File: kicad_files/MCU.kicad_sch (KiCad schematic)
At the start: 27 parts, among them J1 Conn_01x01_Socket, J2 Conn_01x01_Socket, J3 Conn_01x01_Socket, SW1 BOOT BUTTON, SW2 SW_Push, U1 STM32F407VGTx, Y1 LFXTAL036869Reel 8MHz Crystal

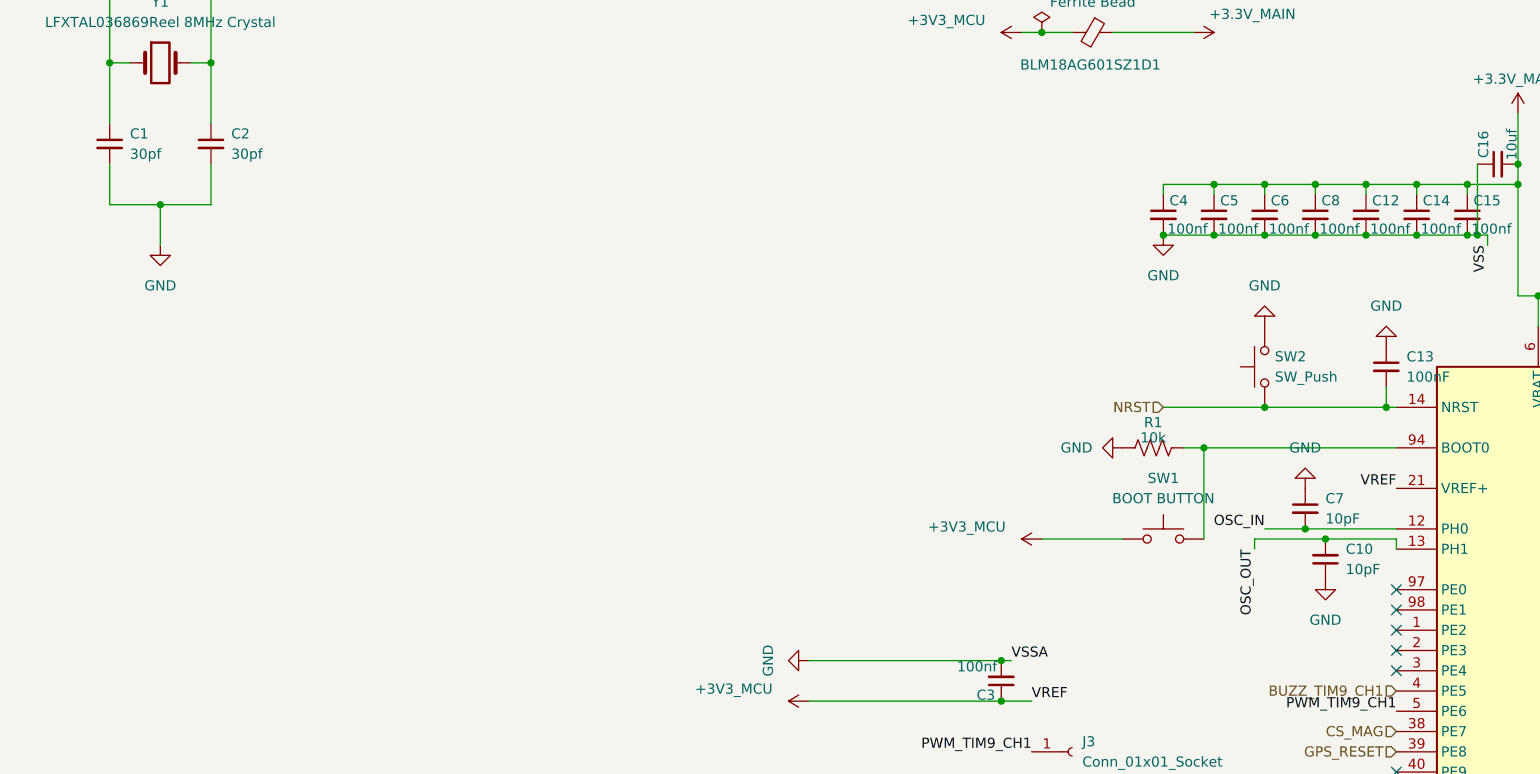
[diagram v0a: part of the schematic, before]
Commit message: rm 10pf caps, add 33pf caps close to mcu pins
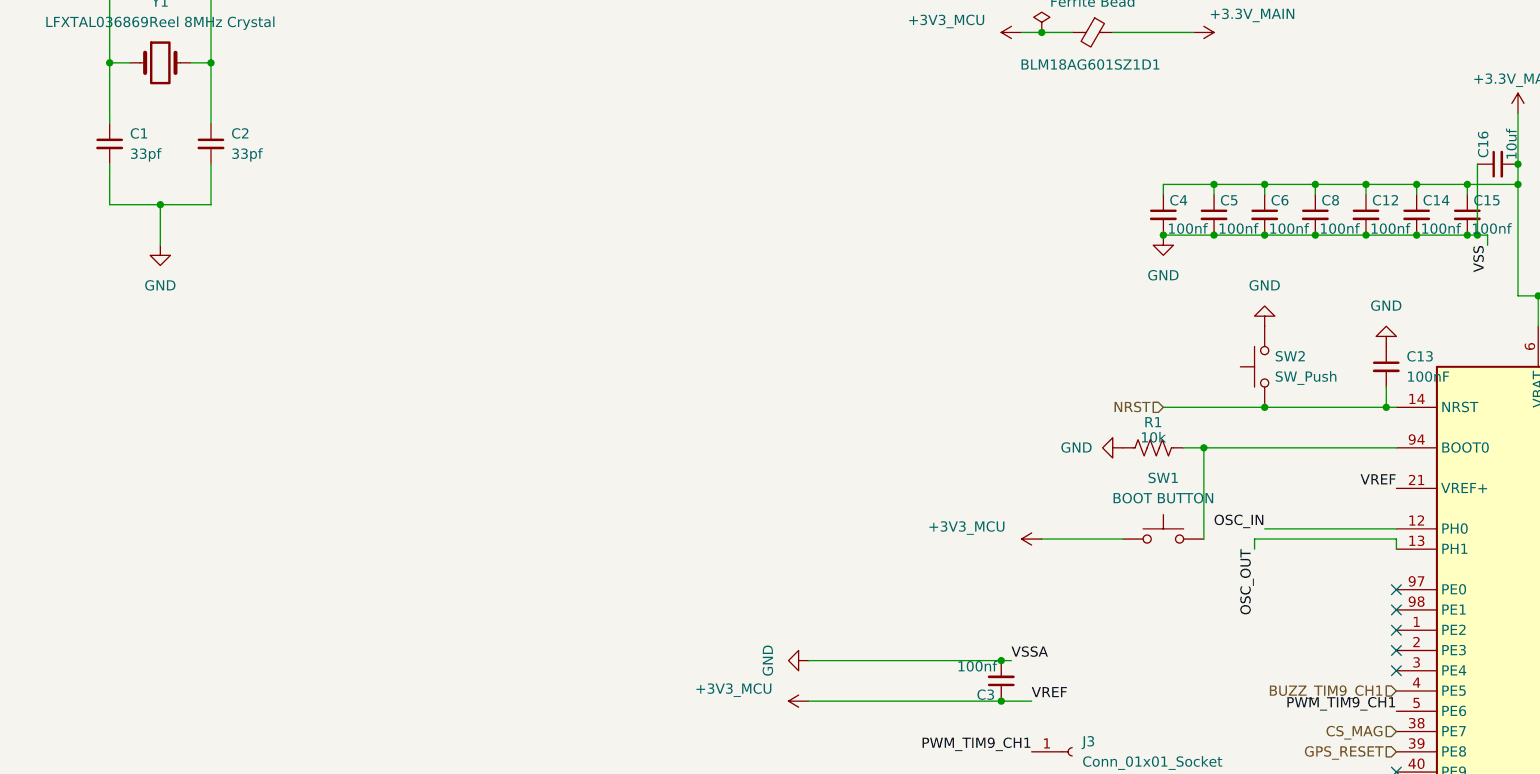
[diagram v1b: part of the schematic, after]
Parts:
- removed C10, C7: 10pF, Capacitor_SMD:C_0402_1005Metric, symbol Device:C_Small
- C1, C2: value 30pf -> 33pf

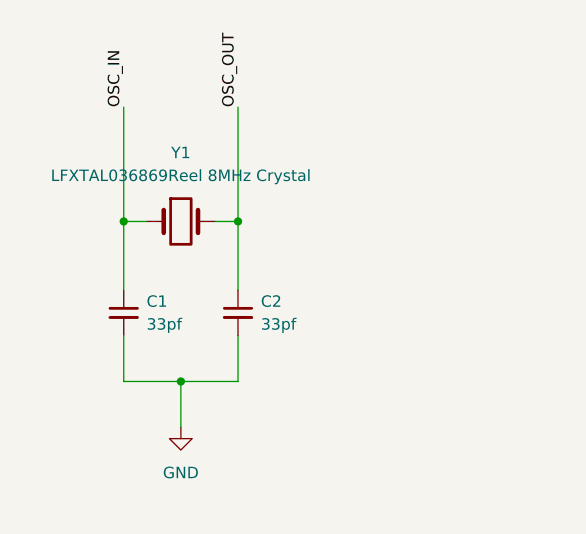
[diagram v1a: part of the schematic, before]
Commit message: replace crystal with smaller, lower esr one, redo footprints, traces
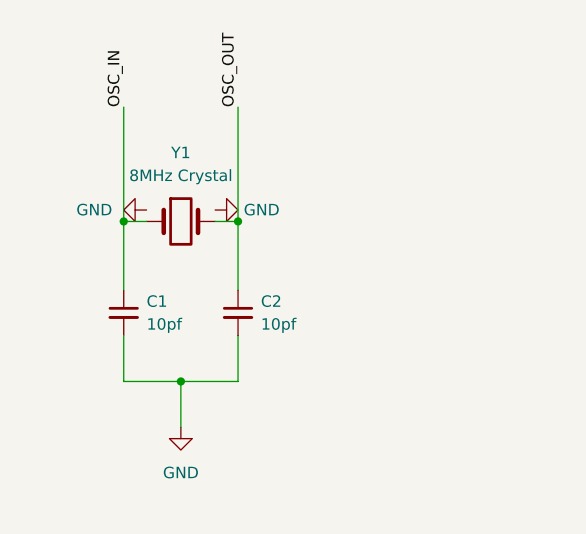
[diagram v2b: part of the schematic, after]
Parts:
- C1, C2: value 33pf -> 10pf
- Y1: value LFXTAL036869Reel 8MHz Crystal -> 8MHz Crystal; footprint Crystal:Crystal_SMD_HC49-SD -> Crystal:Crystal_SMD_3225-4Pin_3.2x2.5mm
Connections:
- net GND: now also Y1.2, Y1.4
- net OSC_OUT: now also Y1.3; no longer Y1.2
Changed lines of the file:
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@@
 			)
 		)
-		(property "Value" "33pf"
+		(property "Value" "10pf"
 			(at 40.64 62.2362 0)
 			(show_name no)
@@
 	)
 	(symbol
+		(lib_id "power:GND")
+		(at 48.26 49.53 90)
+		(unit 1)
+		(body_style 1)
+		(exclude_from_sim no)
+		(in_bom yes)
+		(on_board yes)
+		(in_pos_files yes)
+		(dnp no)
+		(fields_autoplaced yes)
+		(property "Reference" "#PWR010"
+			(at 54.61 49.53 0)
+			(hide yes)
+			(show_name no)
+			(do_not_autoplace no)
+			(effects
+				(font
+					(size 1.27 1.27)
+				)
+			)
+		)
+		(property "Value" "GND"
+			(at 51.435 49.5299 90)
+			(show_name no)
+			(do_not_autoplace no)
+			(effects
+				(font
+					(size 1.27 1.27)
+				)
+				(justify right)
+			)
+		)
+		(property "Footprint" ""
+			(at 48.26 49.53 0)
+			(hide yes)
+			(show_name no)
+			(do_not_autoplace no)
+			(effects
+				(font
+					(size 1.27 1.27)
+				)
+			)
+		)
+		(property "Datasheet" ""
+			(at 48.26 49.53 0)
+			(hide yes)
+			(show_name no)
+			(do_not_autoplace no)
+			(effects
+				(font
+					(size 1.27 1.27)
+				)
+			)
+		)
+		(property "Description" "Power symbol creates a global label with name \"GND\" , ground"
+			(at 48.26 49.53 0)
+			(hide yes)
+			(show_name no)
+			(do_not_autoplace no)
+			(effects
+				(font
+					(size 1.27 1.27)
+				)
+			)
+		)
+		(pin "1"
+		)
+		(instances
+			(project "versorlite"
+				(path "/1a230af0-0a74-48f7-8607-b087121dda49/a6e36be3-aff5-4566-a903-d81edfd88a96"
+					(reference "#PWR010")
+					(unit 1)
+				)
+			)
+		)
+	)
+	(symbol
 		(lib_id "power:+3.3V")
 		(at 173.99 46.99 270)
@@
 	)
 	(symbol
+		(lib_id "power:GND")
+		(at 40.64 49.53 270)
+		(unit 1)
+		(body_style 1)
+		(exclude_from_sim no)
+		(in_bom yes)
+		(on_board yes)
+		(in_pos_files yes)
+		(dnp no)
+		(fields_autoplaced yes)
+		(property "Reference" "#PWR011"
+			(at 34.29 49.53 0)
+			(hide yes)
+			(show_name no)
+			(do_not_autoplace no)
+			(effects
+				(font
+					(size 1.27 1.27)
+				)
+			)
+		)
+		(property "Value" "GND"
+			(at 36.83 49.5299 90)
+			(show_name no)
+			(do_not_autoplace no)
+			(effects
+				(font
+					(size 1.27 1.27)
+				)
+				(justify right)
+			)
+		)
+		(property "Footprint" ""
+			(at 40.64 49.53 0)
+			(hide yes)
+			(show_name no)
+			(do_not_autoplace no)
+			(effects
+				(font
+					(size 1.27 1.27)
+				)
+			)
+		)
+		(property "Datasheet" ""
+			(at 40.64 49.53 0)
+			(hide yes)
+			(show_name no)
+			(do_not_autoplace no)
+			(effects
+				(font
+					(size 1.27 1.27)
+				)
+			)
+		)
+		(property "Description" "Power symbol creates a global label with name \"GND\" , ground"
+			(at 40.64 49.53 0)
+			(hide yes)
+			(show_name no)
+			(do_not_autoplace no)
+			(effects
+				(font
+					(size 1.27 1.27)
+				)
+			)
+		)
+		(pin "1"
+		)
+		(instances
+			(project "versorlite"
+				(path "/1a230af0-0a74-48f7-8607-b087121dda49/a6e36be3-aff5-4566-a903-d81edfd88a96"
+					(reference "#PWR011")
+					(unit 1)
+				)
+			)
+		)
+	)
+	(symbol
 		(lib_id "Connector:Conn_01x01_Socket")
 		(at 158.115 152.4 0)
@@
 			)
 		)
-		(property "Value" "LFXTAL036869Reel 8MHz Crystal"
+		(property "Value" "8MHz Crystal"
 			(at 44.45 45.72 0)
 			(show_name no)
@@
 			)
 		)
-		(property "Footprint" "Crystal:Crystal_SMD_HC49-SD"
+		(property "Footprint" "Crystal:Crystal_SMD_3225-4Pin_3.2x2.5mm"
 			(at 44.45 50.8 0)
 			(hide yes)
@@
 		)
 		(pin "1"
+		)
+		(pin "3"
+		)
+		(pin "4"
 		)
 		(instances
@@
 			)
 		)
-		(property "Value" "33pf"
+		(property "Value" "10pf"
 			(at 53.34 62.2362 0)
 			(show_name no)

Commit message: fix pyro adc
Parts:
- renumbered C12 to C10, C13 to C11, C14 to C12, C15 to C13, C16 to C14, C17 to C15, C18 to C16, C8 to C7, C9 to C8, C11 to C9
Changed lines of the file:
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@@
 		(in_pos_files yes)
 		(dnp no)
-		(property "Reference" "C15"
+		(property "Reference" "C13"
 			(at 209.042 68.072 0)
 			(show_name no)
@@
 			(project "versorlite"
 				(path "/1a230af0-0a74-48f7-8607-b087121dda49/a6e36be3-aff5-4566-a903-d81edfd88a96"
-					(reference "C15")
+					(reference "C13")
 					(unit 1)
 				)
@@
 		(dnp no)
 		(fields_autoplaced yes)
-		(property "Reference" "#PWR06"
+		(property "Reference" "#PWR08"
 			(at 158.75 99.06 0)
 			(hide yes)
@@
 			(project "versorlite"
 				(path "/1a230af0-0a74-48f7-8607-b087121dda49/a6e36be3-aff5-4566-a903-d81edfd88a96"
-					(reference "#PWR06")
+					(reference "#PWR08")
 					(unit 1)
 				)
@@
 		(in_pos_files yes)
 		(dnp no)
-		(property "Reference" "C8"
+		(property "Reference" "C7"
 			(at 189.992 68.072 0)
 			(show_name no)
@@
 			(project "versorlite"
 				(path "/1a230af0-0a74-48f7-8607-b087121dda49/a6e36be3-aff5-4566-a903-d81edfd88a96"
-					(reference "C8")
+					(reference "C7")
 					(unit 1)
 				)
@@
 		(dnp no)
 		(fields_autoplaced yes)
-		(property "Reference" "#PWR01"
+		(property "Reference" "#PWR02"
 			(at 44.45 80.01 0)
 			(hide yes)
@@
 			(project "versorlite"
 				(path "/1a230af0-0a74-48f7-8607-b087121dda49/a6e36be3-aff5-4566-a903-d81edfd88a96"
-					(reference "#PWR01")
+					(reference "#PWR02")
 					(unit 1)
 				)
@@
 		(in_pos_files yes)
 		(dnp no)
-		(property "Reference" "C9"
+		(property "Reference" "C8"
 			(at 184.658 207.772 0)
 			(show_name no)
@@
 			(project "versorlite"
 				(path "/1a230af0-0a74-48f7-8607-b087121dda49/a6e36be3-aff5-4566-a903-d81edfd88a96"
-					(reference "C9")
+					(reference "C8")
 					(unit 1)
 				)
@@
 		(in_pos_files yes)
 		(dnp no)
-		(property "Reference" "#PWR05"
+		(property "Reference" "#PWR07"
 			(at 158.75 110.49 0)
 			(hide yes)
@@
 			(project "versorlite"
 				(path "/1a230af0-0a74-48f7-8607-b087121dda49/a6e36be3-aff5-4566-a903-d81edfd88a96"
-					(reference "#PWR05")
+					(reference "#PWR07")
 					(unit 1)
 				)
@@
 		(in_pos_files yes)
 		(dnp no)
-		(property "Reference" "C17"
+		(property "Reference" "C15"
 			(at 235.712 62.738 0)
 			(show_name no)
@@
 			(project "versorlite"
 				(path "/1a230af0-0a74-48f7-8607-b087121dda49/a6e36be3-aff5-4566-a903-d81edfd88a96"
-					(reference "C17")
+					(reference "C15")
 					(unit 1)
 				)
@@
 		(in_pos_files yes)
 		(dnp no)
-		(property "Reference" "C18"
+		(property "Reference" "C16"
 			(at 235.712 79.248 0)
 			(show_name no)
@@
 			(project "versorlite"
 				(path "/1a230af0-0a74-48f7-8607-b087121dda49/a6e36be3-aff5-4566-a903-d81edfd88a96"
-					(reference "C18")
+					(reference "C16")
 					(unit 1)
 				)
@@
 		(dnp no)
 		(fields_autoplaced yes)
-		(property "Reference" "#PWR010"
+		(property "Reference" "#PWR03"
 			(at 54.61 49.53 0)
 			(hide yes)
@@
 			(project "versorlite"
 				(path "/1a230af0-0a74-48f7-8607-b087121dda49/a6e36be3-aff5-4566-a903-d81edfd88a96"
-					(reference "#PWR010")
+					(reference "#PWR03")
 					(unit 1)
 				)
@@
 		(in_pos_files yes)
 		(dnp no)
-		(property "Reference" "#PWR08"
+		(property "Reference" "#PWR010"
 			(at 170.18 46.99 0)
 			(hide yes)
@@
 			(project "versorlite"
 				(path "/1a230af0-0a74-48f7-8607-b087121dda49/a6e36be3-aff5-4566-a903-d81edfd88a96"
-					(reference "#PWR08")
+					(reference "#PWR010")
 					(unit 1)
 				)
@@
 		(dnp no)
 		(fields_autoplaced yes)
-		(property "Reference" "#PWR011"
+		(property "Reference" "#PWR01"
 			(at 34.29 49.53 0)
 			(hide yes)
@@
 			(project "versorlite"
 				(path "/1a230af0-0a74-48f7-8607-b087121dda49/a6e36be3-aff5-4566-a903-d81edfd88a96"
-					(reference "#PWR011")
+					(reference "#PWR01")
 					(unit 1)
 				)
@@
 		(in_pos_files yes)
 		(dnp no)
-		(property "Reference" "C16"
+		(property "Reference" "C14"
 			(at 210.312 62.738 0)
 			(show_name no)
@@
 			(project "versorlite"
 				(path "/1a230af0-0a74-48f7-8607-b087121dda49/a6e36be3-aff5-4566-a903-d81edfd88a96"
-					(reference "C16")
+					(reference "C14")
 					(unit 1)
 				)
@@
 		(in_pos_files yes)
 		(dnp no)
-		(property "Reference" "C14"
+		(property "Reference" "C12"
 			(at 202.692 68.072 0)
 			(show_name no)
@@
 			(project "versorlite"
 				(path "/1a230af0-0a74-48f7-8607-b087121dda49/a6e36be3-aff5-4566-a903-d81edfd88a96"
-					(reference "C14")
+					(reference "C12")
 					(unit 1)
 				)
@@
 		(in_pos_files yes)
 		(dnp no)
-		(property "Reference" "C11"
+		(property "Reference" "C9"
 			(at 195.072 207.772 0)
 			(show_name no)
@@
 			(project "versorlite"
 				(path "/1a230af0-0a74-48f7-8607-b087121dda49/a6e36be3-aff5-4566-a903-d81edfd88a96"
-					(reference "C11")
+					(reference "C9")
 					(unit 1)
 				)
@@
 		(dnp no)
 		(fields_autoplaced yes)
-		(property "Reference" "#PWR07"
+		(property "Reference" "#PWR09"
 			(at 170.18 78.74 0)
 			(hide yes)
@@
 			(project "versorlite"
 				(path "/1a230af0-0a74-48f7-8607-b087121dda49/a6e36be3-aff5-4566-a903-d81edfd88a96"
-					(reference "#PWR07")
+					(reference "#PWR09")
 					(unit 1)
 				)
@@
 		(in_pos_files yes)
 		(dnp no)
-		(property "Reference" "C12"
+		(property "Reference" "C10"
 			(at 196.342 68.072 0)
 			(show_name no)
@@
 			(project "versorlite"
 				(path "/1a230af0-0a74-48f7-8607-b087121dda49/a6e36be3-aff5-4566-a903-d81edfd88a96"
-					(reference "C12")
+					(reference "C10")
 					(unit 1)
 				)
@@
 		(in_pos_files yes)
 		(dnp no)
-		(property "Reference" "#PWR04"
+		(property "Reference" "#PWR06"
 			(at 156.21 46.99 0)
 			(hide yes)
@@
 			(project "versorlite"
 				(path "/1a230af0-0a74-48f7-8607-b087121dda49/a6e36be3-aff5-4566-a903-d81edfd88a96"
-					(reference "#PWR04")
+					(reference "#PWR06")
 					(unit 1)
 				)
@@
 		(dnp no)
 		(fields_autoplaced yes)
-		(property "Reference" "C13"
+		(property "Reference" "C11"
 			(at 200.66 87.6362 0)
 			(show_name no)
@@
 			(project "versorlite"
 				(path "/1a230af0-0a74-48f7-8607-b087121dda49/a6e36be3-aff5-4566-a903-d81edfd88a96"
-					(reference "C13")
+					(reference "C11")
 					(unit 1)
 				)
@@
 		(dnp no)
 		(fields_autoplaced yes)
-		(property "Reference" "#PWR02"
+		(property "Reference" "#PWR04"
 			(at 119.38 125.73 0)
 			(hide yes)
@@
 			(project "versorlite"
 				(path "/1a230af0-0a74-48f7-8607-b087121dda49/a6e36be3-aff5-4566-a903-d81edfd88a96"
-					(reference "#PWR02")
+					(reference "#PWR04")
 					(unit 1)
 				)
@@
 		(in_pos_files yes)
 		(dnp no)
-		(property "Reference" "#PWR03"
+		(property "Reference" "#PWR05"
 			(at 129.54 130.81 0)
 			(hide yes)
@@
 			(project "versorlite"
 				(path "/1a230af0-0a74-48f7-8607-b087121dda49/a6e36be3-aff5-4566-a903-d81edfd88a96"
-					(reference "#PWR03")
+					(reference "#PWR05")
 					(unit 1)
 				)
@@
 		(dnp no)
 		(fields_autoplaced yes)
-		(property "Reference" "#PWR09"
+		(property "Reference" "#PWR011"
 			(at 182.88 77.47 0)
 			(hide yes)
@@
 			(project "versorlite"
 				(path "/1a230af0-0a74-48f7-8607-b087121dda49/a6e36be3-aff5-4566-a903-d81edfd88a96"
-					(reference "#PWR09")
+					(reference "#PWR011")
 					(unit 1)
 				)
